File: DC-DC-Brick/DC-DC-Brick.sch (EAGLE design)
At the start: 19 parts

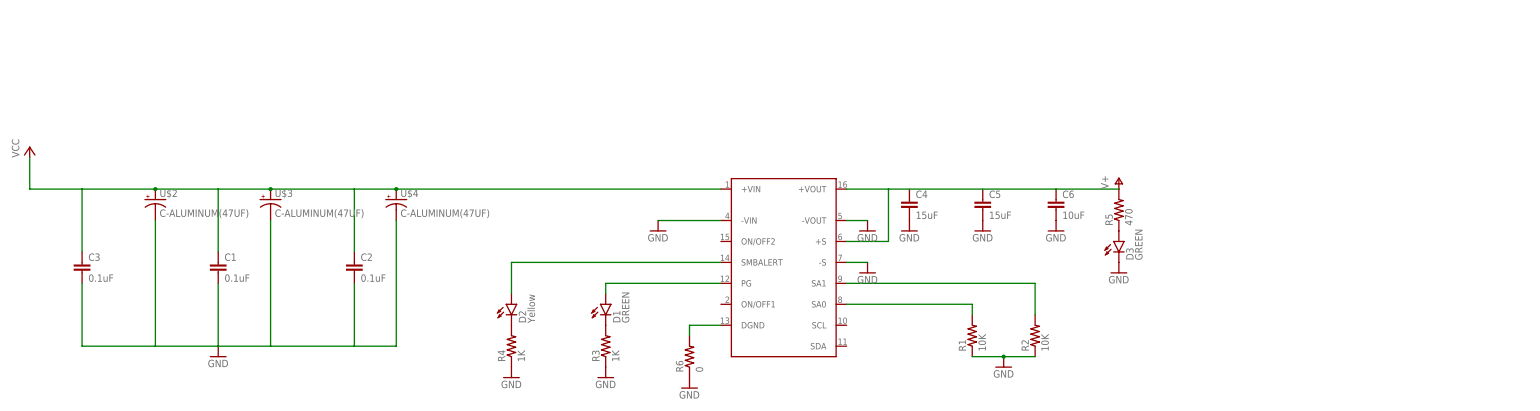
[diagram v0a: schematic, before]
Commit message: Finsh DC-DC Brick Board
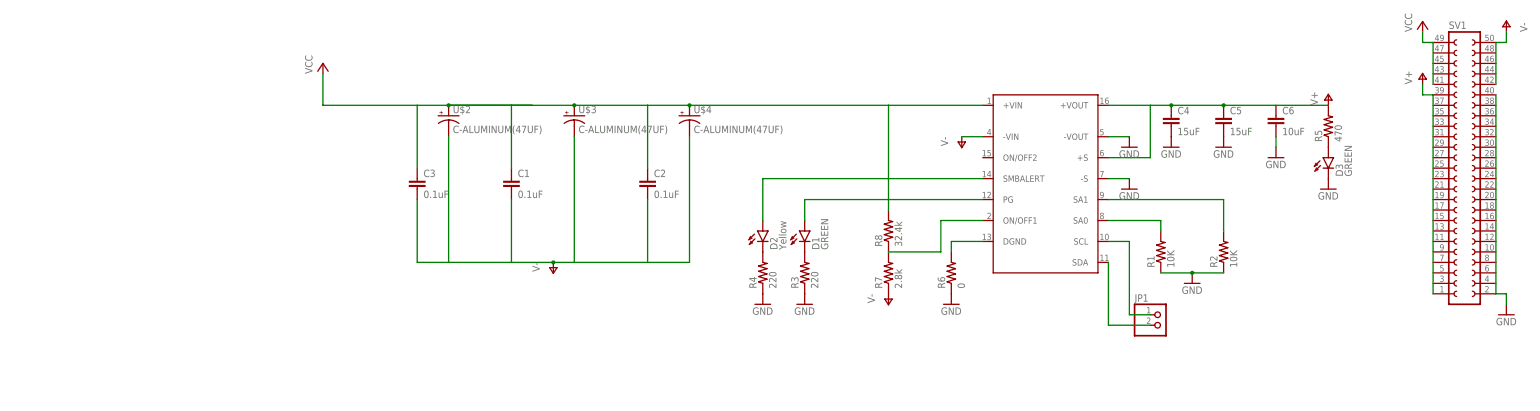
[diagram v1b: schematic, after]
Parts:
- added JP1: (no value), pinhead:PINHD-1X2
- added R7: 2.8k, SparkFun-Resistors:300KOHM-1/10W-1%(0603)
- added R8: 32.4k, SparkFun-Resistors:3.3MOHM-1/10W-1%(0603)
- added SV1: (no value), con-lsta:FE25-2
- R3, R4: value 1K -> 220
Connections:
- new net N$10: JP1.2, U$1.SDA
- new net N$11: JP1.1, U$1.SCL
- new net N$9: R7.2, R8.1, U$1.ON/OFF1
- new net V-: C1.2, C2.2, C3.2, R7.1, SV1.42, SV1.50, U$1.-VIN, U$2.-, U$3.-, U$4.-
- net GND: now also SV1.2, SV1.40; no longer C1.2, C2.2, C3.2, U$1.-VIN, U$2.-, U$3.-, U$4.-
- net V+: now also C4.1, C5.1, SV1.1, SV1.39
- net VCC: now also R8.2, SV1.41, SV1.49
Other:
- moved on the sheet: C1, C2, C3, C4, C5, C6, D1, D2, D3, R1, R2, R3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

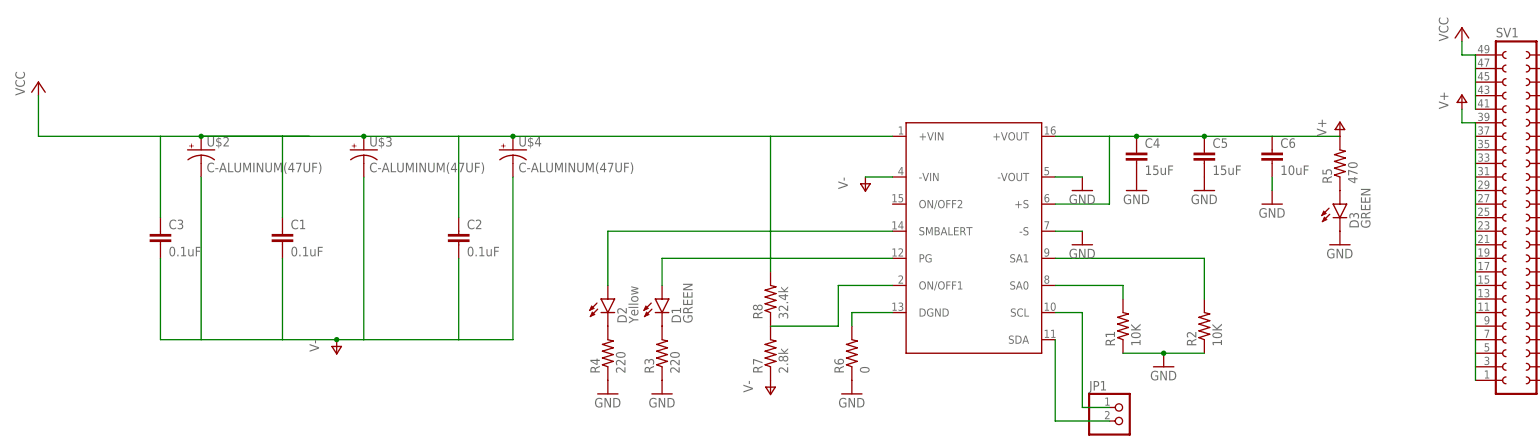
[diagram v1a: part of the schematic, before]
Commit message: Created Board Layout and Changed Schematics
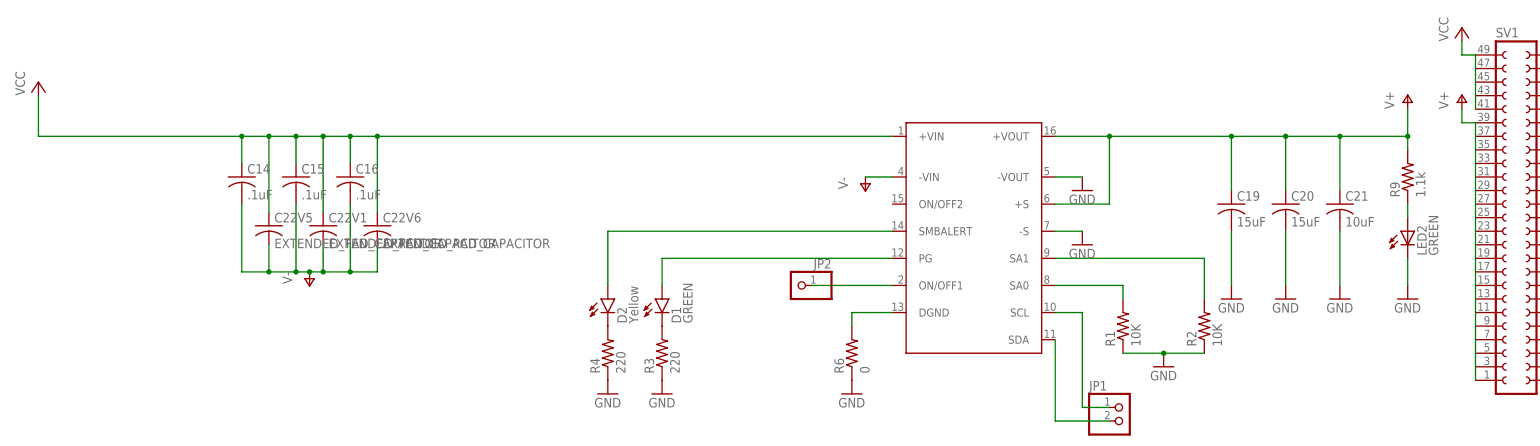
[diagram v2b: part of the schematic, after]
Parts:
- removed C1, C2, C3: 0.1uF, SparkFun-Capacitors:0.1UF-100V-10%(0603)
- removed C4, C5: 15uF, SparkFun-Capacitors:10UF-6.3V-20%(0603)
- removed C6: 10uF, SparkFun-Capacitors:10UF-6.3V-20%(0603)
- removed D3: GREEN, SparkFun-LED:LED-GREEN0603
- removed R5: 470, SparkFun-Resistors:470OHM1/10W1%(0603)
- removed R7: 2.8k, SparkFun-Resistors:300KOHM-1/10W-1%(0603)
- removed R8: 32.4k, SparkFun-Resistors:3.3MOHM-1/10W-1%(0603)
- removed U$2, U$3, U$4: C-ALUMINUM(47UF), PowerComponents:C-ALUMINUM(47UF)
- added C14, C15, C16: .1uF, rcl:C-USC0603
- added C19, C20: 15uF, rcl:C-USC3216
- added C21: 10uF, rcl:C-USC0603
- added C22V1, C22V5, C22V6: EXTENDED_PAD_CAPACITOR, ExtendedPadCap:EXTENDED_PAD_CAPACITOR
- added JP2: (no value), pinhead:PINHD-1X1
- added LED2: GREEN, SparkFun:LED0603
- added R9: 1.1k, resistor:R-US_R1206
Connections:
- removed net N$8: D3.A, R5.1
- new net +12V1: C19.1, C20.1, C21.1, R9.2, U$1.+S, U$1.+VOUT
- new net N$12: LED2.A, R9.1
- net GND: now also C19.2, C20.2, C21.2, LED2.C; no longer C4.2, C5.2, C6.2, D3.C
- net N$9: now also JP2.1; no longer R7.2, R8.1
- net V+: no longer C4.1, C5.1, C6.1, R5.2, U$1.+S, U$1.+VOUT
- net V-: now also C14.2, C15.2, C16.2, C22V1.4, C22V5.4, C22V6.4; no longer C1.2, C2.2, C3.2, R7.1, U$2.-, U$3.-, U$4.-
- net VCC: now also C14.1, C15.1, C16.1, C22V1.3, C22V5.3, C22V6.3; no longer C1.1, C2.1, C3.1, R8.2, U$2.+, U$3.+, U$4.+

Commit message: Worked on Board Layout
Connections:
- removed net V+: SV1.1, SV1.39
- net +12V1: now also SV1.1, SV1.11, SV1.13, SV1.15, SV1.17, SV1.19, SV1.21, SV1.23, SV1.25, SV1.27, SV1.29, SV1.3, SV1.31, SV1.33, SV1.35, SV1.37, SV1.39, SV1.5, SV1.7, SV1.9
- net GND: now also D1.C, D2.C, SV1.10, SV1.12, SV1.14, SV1.16, SV1.18, SV1.20, SV1.22, SV1.24, SV1.26, SV1.28, SV1.30, SV1.32, SV1.34, SV1.36, SV1.38, SV1.4, SV1.6, SV1.8; no longer R3.1, R4.1
- net N$4: now also D1.A, R3.1; no longer D1.C, R3.2
- net N$5: now also D2.A, R4.1; no longer D2.C, R4.2
- net N$6: now also R4.2; no longer D2.A
- net N$7: now also R3.2; no longer D1.A
- net V-: now also SV1.44, SV1.46, SV1.48
- net VCC: now also SV1.43, SV1.45, SV1.47
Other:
- moved on the sheet: D1, D2, R3, R4

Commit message: Worked on Board Layout
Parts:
- removed JP1: (no value), pinhead:PINHD-1X2
- removed JP2: (no value), pinhead:PINHD-1X1
- removed SV1: (no value), con-lsta:FE25-2
- added U$2: POWERBRICKCONNECTOR, newConnector:POWERBRICKCONNECTOR
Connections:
- removed net N$10: JP1.2, U$1.SDA
- new net N$8: U$1.SDA, U$2G$2.4
- net +12V1: now also U$2G$1.1, U$2G$1.11, U$2G$1.13, U$2G$1.15, U$2G$1.17, U$2G$1.19, U$2G$1.21, U$2G$1.23, U$2G$1.25, U$2G$1.27, U$2G$1.29, U$2G$1.3, U$2G$1.31, U$2G$1.33, U$2G$1.35, U$2G$1.37, U$2G$1.39, U$2G$1.5, U$2G$1.7, U$2G$1.9; no longer SV1.1, SV1.11, SV1.13, SV1.15, SV1.17, SV1.19, SV1.21, SV1.23, SV1.25, SV1.27, SV1.29, SV1.3, SV1.31, SV1.33, SV1.35, SV1.37, SV1.39, SV1.5, SV1.7, SV1.9
- net GND: now also U$2G$1.10, U$2G$1.12, U$2G$1.14, U$2G$1.16, U$2G$1.18, U$2G$1.2, U$2G$1.20, U$2G$1.22, U$2G$1.24, U$2G$1.26, U$2G$1.28, U$2G$1.30, U$2G$1.32, U$2G$1.34, U$2G$1.36, U$2G$1.38, U$2G$1.4, U$2G$1.40, U$2G$1.6, U$2G$1.8; no longer SV1.10, SV1.12, SV1.14, SV1.16, SV1.18, SV1.2, SV1.20, SV1.22, SV1.24, SV1.26, SV1.28, SV1.30, SV1.32, SV1.34, SV1.36, SV1.38, SV1.4, SV1.40, SV1.6, SV1.8
- net N$11: now also U$2G$2.3; no longer JP1.1
- net N$9: now also U$2G$2.1; no longer JP2.1
- net V-: now also U$2G$1.42, U$2G$1.44, U$2G$1.46, U$2G$1.48, U$2G$1.50; no longer SV1.42, SV1.44, SV1.46, SV1.48, SV1.50
- net VCC: now also U$2G$1.41, U$2G$1.43, U$2G$1.45, U$2G$1.47, U$2G$1.49; no longer SV1.41, SV1.43, SV1.45, SV1.47, SV1.49

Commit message: Worked on DC-DC Board layout
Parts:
- removed U$2: POWERBRICKCONNECTOR, newConnector:POWERBRICKCONNECTOR
- added U$3: POWER-BRICK-CONNECTOR, MotherboardParts:POWER-BRICK-CONNECTOR
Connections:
- removed net +12V1: C19.1, C20.1, C21.1, R9.2, U$1.+S, U$1.+VOUT, U$2G$1.1, U$2G$1.11, U$2G$1.13, U$2G$1.15, U$2G$1.17, U$2G$1.19, U$2G$1.21, U$2G$1.23, U$2G$1.25, U$2G$1.27, U$2G$1.29, U$2G$1.3, U$2G$1.31, U$2G$1.33, U$2G$1.35, U$2G$1.37, U$2G$1.39, U$2G$1.5, U$2G$1.7, U$2G$1.9
- removed net N$11: U$1.SCL, U$2G$2.3
- new net N$10: U$1.SCL, U$3.SCL
- new net V+: C19.1, C20.1, C21.1, R9.2, U$1.+S, U$1.+VOUT, U$3.12V+
- net GND: now also U$3.12V-; no longer U$2G$1.10, U$2G$1.12, U$2G$1.14, U$2G$1.16, U$2G$1.18, U$2G$1.2, U$2G$1.20, U$2G$1.22, U$2G$1.24, U$2G$1.26, U$2G$1.28, U$2G$1.30, U$2G$1.32, U$2G$1.34, U$2G$1.36, U$2G$1.38, U$2G$1.4, U$2G$1.40, U$2G$1.6, U$2G$1.8
- net N$8: now also U$3.SDA; no longer U$2G$2.4
- net N$9: now also U$3.ON/OFF; no longer U$2G$2.1
- net V-: now also U$3.48V-; no longer U$2G$1.42, U$2G$1.44, U$2G$1.46, U$2G$1.48, U$2G$1.50
- net VCC: now also U$3.48V+; no longer U$2G$1.41, U$2G$1.43, U$2G$1.45, U$2G$1.47, U$2G$1.49

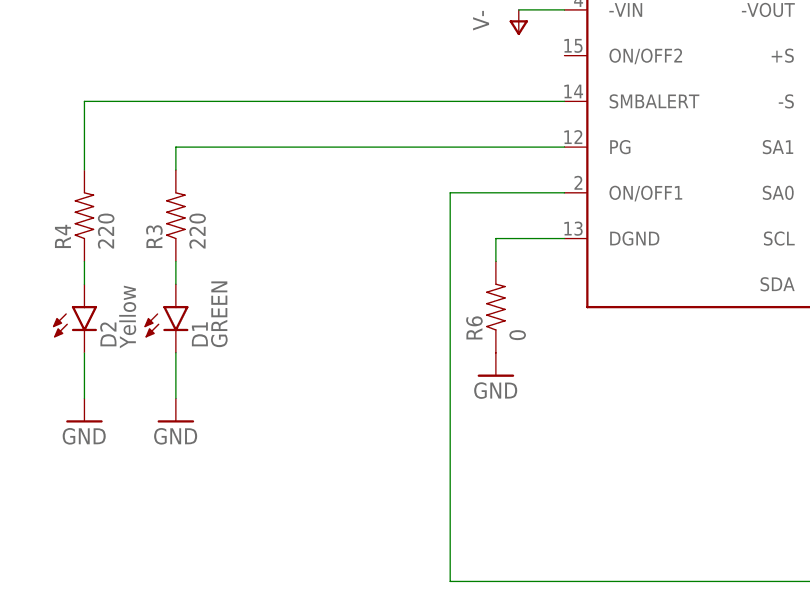
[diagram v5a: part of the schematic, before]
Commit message: Fixed some routing and added resistor
Added resistor between ON/OFF pin and V-. The resistor's value is not
necessarily the value we will end up using.
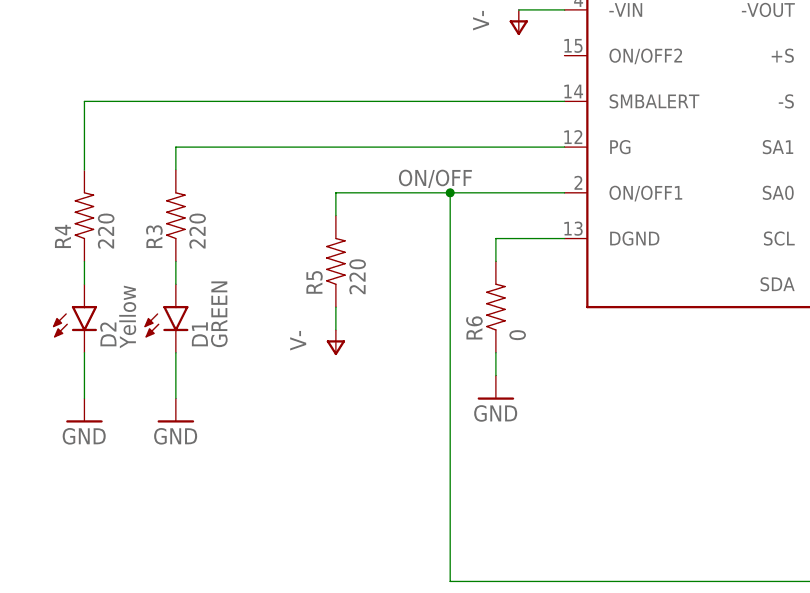
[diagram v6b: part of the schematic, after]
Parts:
- added R5: 220, SparkFun-Resistors:1KOHM-1/10W-1%(0603)
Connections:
- removed net N$9: U$1.ON/OFF1, U$3.ON/OFF
- new net ON/OFF: R5.2, U$1.ON/OFF1, U$3.ON/OFF
- net V-: now also R5.1
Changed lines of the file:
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@@
 <part name="GND8" library="supply1" deviceset="GND" device=""/>
 <part name="P-3" library="supply1" deviceset="V-" device=""/>
+<part name="R5" library="SparkFun-Resistors" deviceset="1KOHM-1/10W-1%(0603)" device="" value="220"/>
+<part name="P-4" library="supply1" deviceset="V-" device=""/>
 </parts>
 <sheets>
@@
 <instance part="GND7" gate="1" x="266.7" y="142.24"/>
 <instance part="R6" gate="G$1" x="223.52" y="121.92" rot="R90"/>
-<instance part="GND12" gate="1" x="223.52" y="114.3"/>
+<instance part="GND12" gate="1" x="223.52" y="111.76"/>
 <instance part="FRAME1" gate="G$1" x="0" y="0"/>
 <instance part="P-2" gate="1" x="226.06" y="152.4"/>
@@
 <instance part="GND8" gate="1" x="292.1" y="78.74"/>
 <instance part="P-3" gate="1" x="292.1" y="93.98"/>
+<instance part="R5" gate="G$1" x="205.74" y="127" rot="R90"/>
+<instance part="P-4" gate="1" x="205.74" y="116.84"/>
 </instances>
 <busses>
@@
 <pinref part="R6" gate="G$1" pin="1"/>
 <pinref part="GND12" gate="1" pin="GND"/>
+<wire x1="223.52" y1="114.3" x2="223.52" y2="116.84" width="0.1524" layer="91"/>
 </segment>
 <segment>
@@
 <wire x1="289.56" y1="96.52" x2="292.1" y2="96.52" width="0.1524" layer="91"/>
 </segment>
+<segment>
+<pinref part="R5" gate="G$1" pin="1"/>
+<pinref part="P-4" gate="1" pin="V-"/>
+<wire x1="205.74" y1="121.92" x2="205.74" y2="119.38" width="0.1524" layer="91"/>
+</segment>
 </net>
 <net name="N$12" class="0">
@@
 </segment>
 </net>
-<net name="N$9" class="0">
+<net name="ON/OFF" class="0">
 <segment>
 <pinref part="U$1" gate="G$1" pin="ON/OFF1"/>
@@
 <pinref part="U$3" gate="G$1" pin="ON/OFF"/>
 <wire x1="218.44" y1="91.44" x2="264.16" y2="91.44" width="0.1524" layer="91"/>
-</segment>
-</net>
+<pinref part="R5" gate="G$1" pin="2"/>
+<wire x1="218.44" y1="134.62" x2="205.74" y2="134.62" width="0.1524" layer="91"/>
+<wire x1="205.74" y1="134.62" x2="205.74" y2="132.08" width="0.1524" layer="91"/>
+<junction x="218.44" y="134.62"/>
+<label x="220.98" y="137.16" size="1.778" layer="95" rot="R180"/>
+</segment>
+</net>
